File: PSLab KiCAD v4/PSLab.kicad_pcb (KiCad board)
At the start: 4 copper layers, 99 x 53.3 mm, 152 parts, among them CON1 USB-MINI-B, J1 Programmer, J10 GND, J11 Vbus, J12 Sensors, J13 D+, J14 D-, J2 SQRs, J3 LA, J4 OSC_Pins, J5 Sin, J6 I2C, J7 IDs, J8 TX_RX_ES, J9 Test_Vs, P1 Power_Sources, P7 NRF, Q1 MMBT3906, Q2 MMBT3904, Q3 MMBT3906, U1 MCP2200, U10 TL082, U11 6S21, U12 6S21, U13 TL082, U15 ESP8266, U16 TL082, U2 74HC126, U3 PIC24EP256GP204, U4 TC1240A, U5 7660, U6 LM1117-3.3, U7 LM324, U8 TL082, U9 MCP4728, X1 8MHz, Y1 12MHz

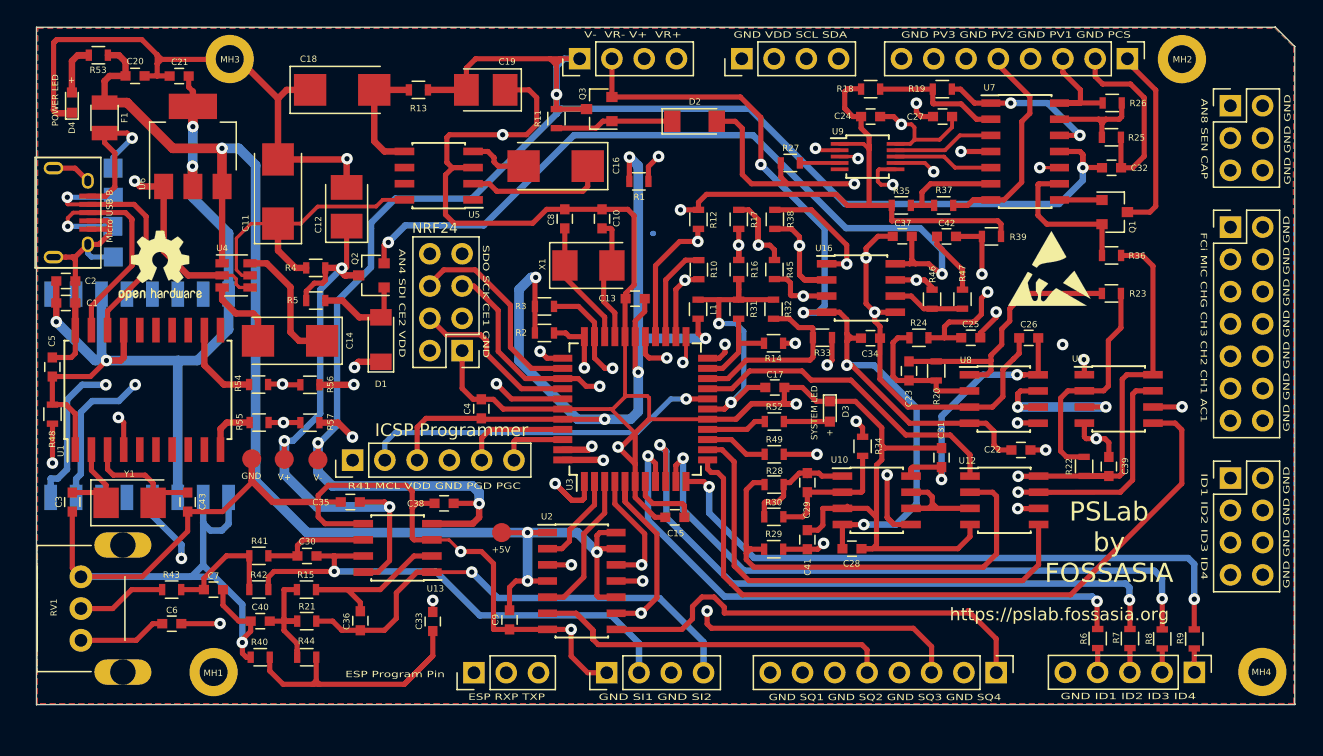
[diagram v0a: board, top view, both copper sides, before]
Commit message: Updated docs with new layout
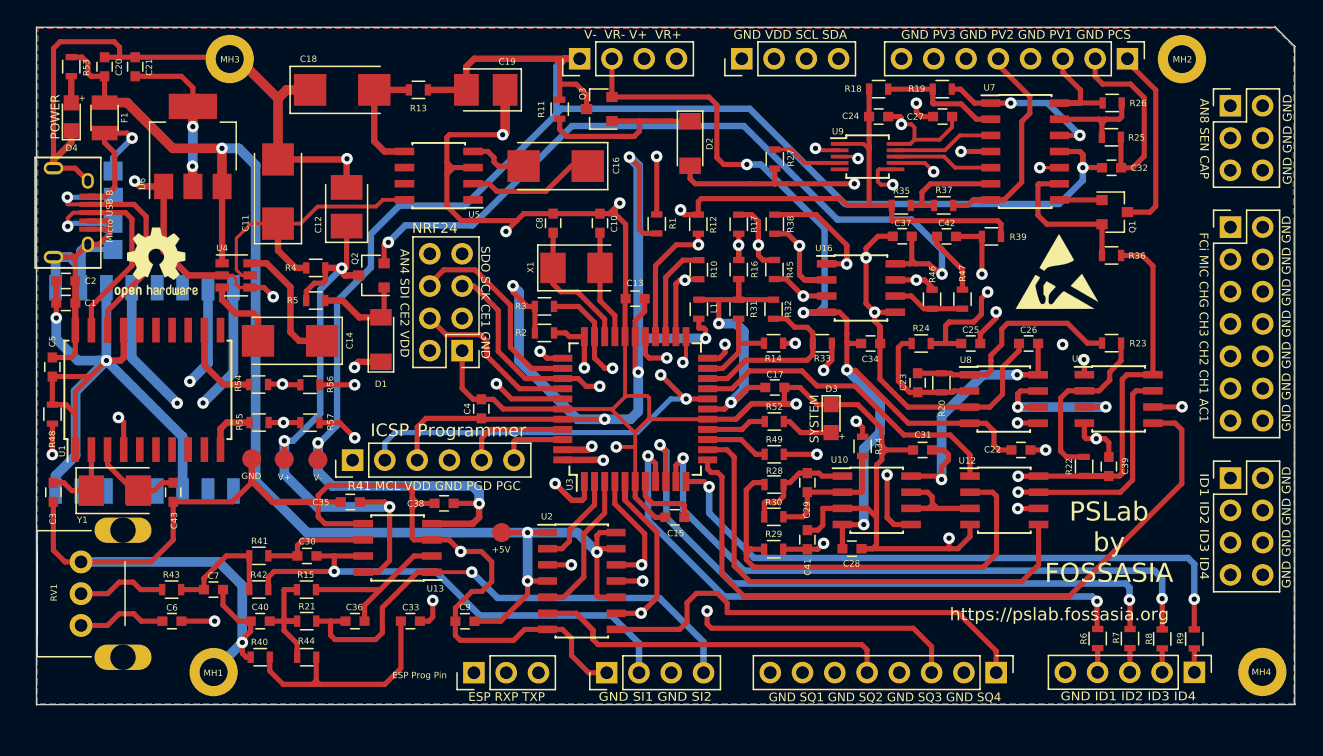
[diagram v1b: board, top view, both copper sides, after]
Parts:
- C10, C8: value 15pF -> 33pF
- C3, C43: value 22p -> 33p
- D3, D4: footprint LEDs:LED_0603 -> LEDs:LED_0805
- R48: value 4.7k -> 5k1
- R49: value 560 -> 200
- X1: value 8MHz -> 12MHz
- moved R23 3.91 mm to (175.6, 85.1)
- moved R1 3.63 mm to (139.8, 75.8), turned to 90 degrees
- moved C21 3.54 mm to (98.7, 63.4), turned to 90 degrees
- moved C9 3.51 mm to (124.7, 107.0), turned to 0 degrees
- moved C20 2.51 mm to (96.3, 63.4), turned to 270 degrees
- moved R53 2.31 mm to (93.7, 63.4), turned to 90 degrees
- moved D2 1.78 mm to (142.4, 69.4), turned to 270 degrees
- moved C33 1.76 mm to (120.4, 107.0), turned to 180 degrees
- moved C3 1.68 mm to (92.3, 96.9)
- moved C31 1.61 mm to (160.7, 93.5), turned to 0 degrees
- moved Y1 1.51 mm to (97.1, 96.7)
- moved C43 1.38 mm to (101.7, 96.9)
- moved R27 1.26 mm to (149.1, 70.6), turned to 270 degrees
- moved RV1 1.17 mm to (94.5, 102.3)
- moved C23 1.15 mm to (160.3, 88.2)
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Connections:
- L1 pad 1: AVdd -> Vdd
- L1 pad 2: Vdd -> AVdd
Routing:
- net GND: track 851.2 -> 764.4 mm, vias 16 -> 19
- net V-: track 168.2 -> 145.6 mm, vias 4 -> 3
- net /RxD: track 94.4 -> 73.4 mm
- net /ESPROG: track 33.5 -> 49.4 mm
- net V+: track 134.8 -> 147.2 mm
- net /ETxD: track 37.2 -> 26.4 mm
- net VR-: track 87.8 -> 77.6 mm
- net Vdd: track 211.8 -> 221.6 mm
- net Net-(D2-Pad1): track 9.35 -> 19.0 mm
- net /SQR3: track 39.0 -> 29.6 mm
- net SINE1: track 48.7 -> 40.0 mm
- net /ERxD: track 33.3 -> 24.7 mm
- net Net-(R19-Pad2): track 20.4 -> 13.2 mm
- net AN4: track 38.7 -> 32.5 mm
- net VR+: track 123.5 -> 129.0 mm
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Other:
- rule trace_min: 0.15 -> 0.2
- rule via_min_size: 0.3 -> 0.4
- board text added: "4th Rev @ 29 Jan '18"
- board text added: "ESP Prog Pin"
- board text added: "ICSP"
- board text added: "POWER"
- board text added: "Pin 1"
- board text added: "Programmer"
- board text added: "SYSTEM"
- board text removed: "4th Rev @ 29 Jan 18"
- board text removed: "ESP Program Pin"
- board text removed: "ICSP Programmer"
- board text removed: "POWER LED"
- board text removed: "SYSTEM LED"

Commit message: New layout with pins adjusted + Bluetooth
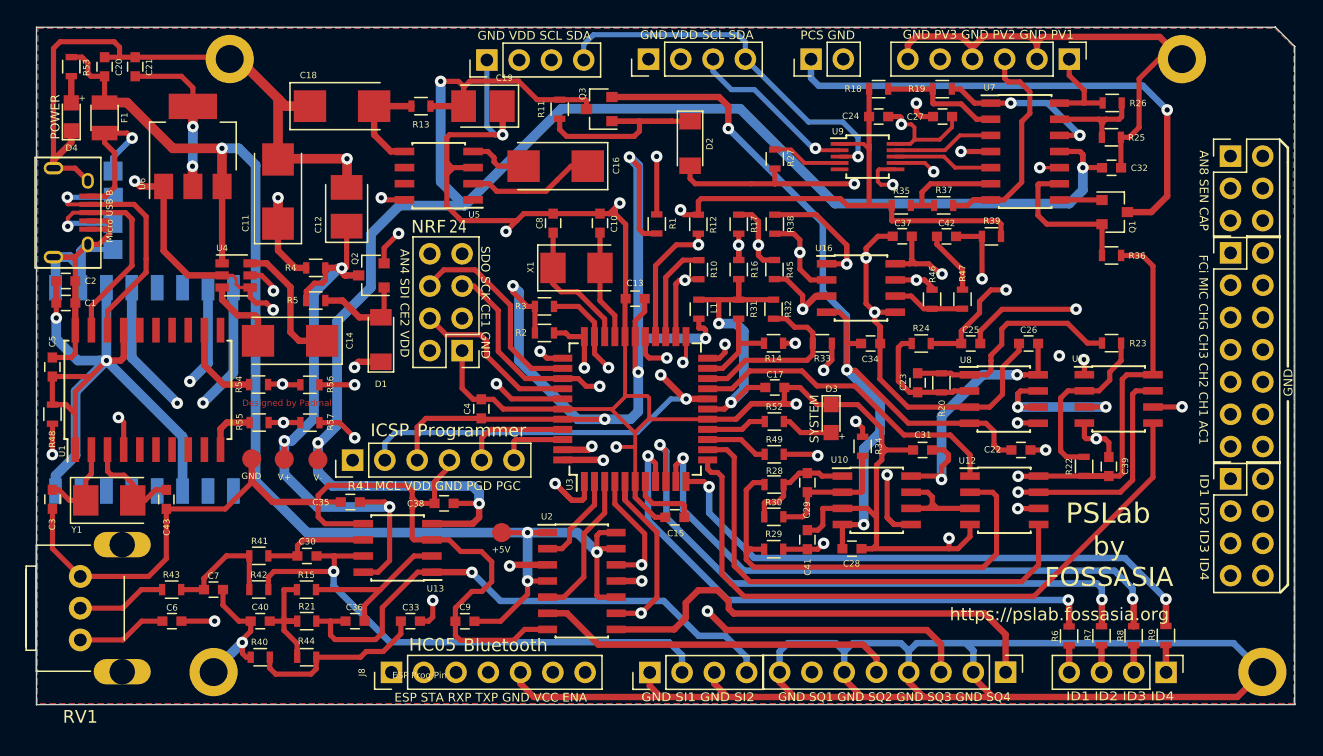
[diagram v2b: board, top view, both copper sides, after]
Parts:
- removed P1: Power_Sources, Pin_Headers:Pin_Header_Straight_1x08_Pitch2.54mm
- removed REF***: ESD-Logo_6.6x6mm_SilkScreen, Symbols:ESD-Logo_6.6x6mm_SilkScreen
- removed REF***: OSHW-Logo2_7.3x6mm_SilkScreen, Symbols:OSHW-Logo2_7.3x6mm_SilkScreen
- added J15: PCs, Pin_Headers:Pin_Header_Straight_1x02_Pitch2.54mm, F.Cu at (151.9, 62.8)
- added J16: I2C-2, Pin_Headers:Pin_Header_Straight_1x04_Pitch2.54mm, F.Cu at (139.1, 62.8)
- J3: footprint Pin_Headers:Pin_Header_Straight_1x05_Pitch2.54mm -> Pin_Headers:Pin_Header_Straight_1x04_Pitch2.54mm
- J6: value I2C -> I2C-1
- J8: value TX_RX_ES -> Conn_01x07; footprint Pin_Headers:Pin_Header_Straight_1x03_Pitch2.54mm -> Pin_Headers:Pin_Header_Straight_1x07_Pitch2.54mm
- J9: value Test_Vs -> PVs; footprint Pin_Headers:Pin_Header_Straight_1x04_Pitch2.54mm -> Pin_Headers:Pin_Header_Straight_1x06_Pitch2.54mm
- RV1: value 100K -> POT
- moved J9 38.5 mm to (172.2, 62.8), turned to 270 degrees
- moved J6 20.1 mm to (126.4, 62.9)
- moved J8 6.49 mm to (118.9, 111.0)
- moved J12 3.96 mm to (184.9, 70.4)
- moved J5 3.39 mm to (139.2, 111.0)
- moved R8 2.26 mm to (177.3, 108.2)
- moved R6 2.26 mm to (172.2, 108.2)
- moved R7 2.25 mm to (174.8, 108.2)
- moved R9 2.25 mm to (179.8, 108.1)
- moved J3 2.23 mm to (179.8, 111.0)
- moved J4 2.03 mm to (184.9, 78.0)
- moved C19 1.30 mm to (126.1, 66.5)
- moved R13 1.30 mm to (121.2, 66.5)
- moved C18 1.28 mm to (115.0, 66.5)
- moved RV1 1.14 mm to (94.4, 103.5)
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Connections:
- J8 pad 2: /RxD -> (no net)
- J8 pad 3: /TxD -> /RxD
- J9 pad 1: V- -> PVS1
- J9 pad 2: VR- -> GND
- J9 pad 3: V+ -> PVS2
- J9 pad 4: VR+ -> GND
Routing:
- net AN8: track 61.6 -> 121.6 mm
- net /SEN: track 56.1 -> 88.8 mm
- net PCS: track 15.0 -> 47.3 mm, vias 0 -> 1
- net VR+: track 129.0 -> 104.6 mm
- net SDA: track 50.1 -> 70.1 mm
- net SCL: track 46.0 -> 65.8 mm
- net GND: track 764.4 -> 780.1 mm, vias 19 -> 18
- net V+: track 147.2 -> 135.7 mm
- net +5V: track 107.4 -> 115.8 mm
- net /SQR1: track 26.6 -> 34.7 mm
- net Vdd: track 221.6 -> 228.9 mm
- net /ESPROG: track 49.4 -> 42.9 mm
- net CS.CH1: track 57.1 -> 52.5 mm
- net Net-(C33-Pad2): track 18.7 -> 14.2 mm
- net /ID4: track 49.0 -> 44.9 mm
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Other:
- board text added: "24"
- board text added: "5th Rev @ 13 Apr '18"
- board text added: "Bluetooth"
- board text added: "Designed by Padmal"
- board text added: "ESP STA RXP TXP GND VCC ENA"
- board text added: "GND PV3 GND PV2 GND PV1"
- board text added: "HC05"
- board text added: "NRF"
- board text added: "PCS GND"
- board text added: "PSLab"
- board text added: "by FOSSASIA"
- board text removed: "4th Rev @ 29 Jan '18"
- board text removed: "ESP RXP TXP"
- board text removed: "GND GND GND"
- board text removed: "GND GND GND GND"
- board text removed: "GND GND GND GND GND GND GND"
- board text removed: "GND ID1 ID2 ID3 ID4"
- board text removed: "GND PV3 GND PV2 GND PV1 GND PCS"
- board text removed: "NRF24"
- board text removed: "PSLab by FOSSASIA"
- board text removed: "V- VR- V+ VR+"

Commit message: Refined BOM Sheet
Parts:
- removed J12: Sensors, Pin_Headers:Pin_Header_Straight_2x03_Pitch2.54mm
- removed J5: Sin, Pin_Headers:Pin_Header_Straight_1x04_Pitch2.54mm
- removed J7: IDs, Pin_Headers:Pin_Header_Straight_2x04_Pitch2.54mm
- added REF***: ESD-Logo_6.6x6mm_SilkScreen, Symbols:ESD-Logo_6.6x6mm_SilkScreen, F.Cu at (170.9, 79.6)
- added REF***: OSHW-Logo2_7.3x6mm_SilkScreen, Symbols:OSHW-Logo2_7.3x6mm_SilkScreen, F.Cu at (100.5, 78.7)
- J2: value SQRs -> DoublePins; footprint Pin_Headers:Pin_Header_Straight_1x08_Pitch2.54mm -> Pin_Headers:Pin_Header_Straight_2x14_Pitch2.54mm
- J4: value OSC_Pins -> Outputs; footprint Pin_Headers:Pin_Header_Straight_2x07_Pitch2.54mm -> Pin_Headers:Pin_Header_Straight_1x12_Pitch2.54mm
- MH1, MH2, MH3, MH4: footprint Mounting_Holes:MountingHole_2.2mm_M2_ISO14580_Pad -> Mounting_Holes:MountingHole_3.2mm_M3_DIN965_Pad
- moved J4 56.4 mm to (139.2, 111.0), turned to 90 degrees
- moved C15 55.4 mm to (98.7, 63.4), turned to 270 degrees
- moved C21 55.3 mm to (141.2, 98.8), turned to 0 degrees
- moved J2 44.3 mm to (184.9, 70.4), turned to 0 degrees
- moved Y1 0.91 mm to (97.2, 96.8)
- moved RV1 0.89 mm to (94.4, 102.6)
- moved C43 0.76 mm to (101.5, 96.7)
- moved C3 0.60 mm to (92.3, 96.8)
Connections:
- C15 pad 1: Net-(C15-Pad1) -> GND
- C15 pad 2: GND -> Vdd
- C21 pad 1: Vdd -> GND
- C21 pad 2: GND -> Net-(C21-Pad2)
- J2 pad 1: /SQR4 -> AN8
- J2 pad 3: /SQR3 -> SEN
- J2 pad 5: /SQR2 -> CAP
- J2 pad 7: /SQR1 -> FCin
- J3 pad 1: Net-(J3-Pad1) -> IDD
- J3 pad 2: Net-(J3-Pad2) -> IDC
- J3 pad 3: Net-(J3-Pad3) -> IDB
- J3 pad 4: Net-(J3-Pad4) -> IDA
- J4 pad 1: FCin -> GND
- J4 pad 10: GND -> SQR3
- J4 pad 11: CH1 -> GND
- J4 pad 12: GND -> SQR4
- J4 pad 2: GND -> SINE1
- J4 pad 3: MIC -> GND
- J4 pad 4: GND -> SINE2
- J4 pad 5: CH3.GAIN -> GND
- J4 pad 6: GND -> SQR1
- J4 pad 7: CH3 -> GND
- J4 pad 8: GND -> SQR2
- J4 pad 9: CH2 -> GND
- R10 pad 1: /CAP -> CAP
- R12 pad 2: /SEN -> SEN
- R6 pad 1: Net-(J3-Pad4) -> IDA
- R7 pad 1: Net-(J3-Pad3) -> IDB
- R8 pad 1: Net-(J3-Pad2) -> IDC
- R9 pad 1: Net-(J3-Pad1) -> IDD
- U2 pad 11: /SQR3 -> SQR3
- U2 pad 3: /SQR1 -> SQR1
- U2 pad 6: /SQR2 -> SQR2
- U2 pad 8: /SQR4 -> SQR4
- U3 pad 24: /CAP -> CAP
- U3 pad 26: /SEN -> SEN
- U3 pad 7: Net-(C15-Pad1) -> Net-(C21-Pad2)
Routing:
- net SEN: track 0.00 -> 88.8 mm, vias 0 -> 1
- net /SEN: track 88.8 -> 0.00 mm, vias 1 -> 0
- net CAP: track 0.00 -> 52.0 mm, vias 0 -> 1
- net /CAP: track 52.0 -> 0.00 mm, vias 1 -> 0
- net SQR4: track 0.00 -> 37.4 mm
- net /SQR4: track 37.4 -> 0.00 mm
- net SQR1: track 0.00 -> 34.7 mm, vias 0 -> 1
- net /SQR1: track 34.7 -> 0.00 mm, vias 1 -> 0
- net SQR3: track 0.00 -> 29.8 mm, vias 0 -> 2
- net /SQR3: track 29.8 -> 0.00 mm, vias 2 -> 0
- net SQR2: track 0.00 -> 28.5 mm
- net /SQR2: track 28.5 -> 0.00 mm
- net Net-(J3-Pad4): track 26.5 -> 0.00 mm
- net IDA: track 0.00 -> 26.5 mm
- net GND: track 780.1 -> 803.0 mm
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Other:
- board text added: "5th Rev @ 21 Apr '18"
- board text added: "Analog"
- board text added: "Digital"
- board text removed: "5th Rev @ 13 Apr '18"
